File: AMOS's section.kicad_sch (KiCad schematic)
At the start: 0 parts

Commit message: Add Charging circuit and USB integration
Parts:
- added C1, C12: 4.7u, symbol Device:C_Small
- added D2: Red, symbol Device:LED_Small_Filled
- added D3: Green, symbol Device:LED_Small
- added J1: USB_C_Receptacle_PowerOnly_6P, Connector_USB:USB_C_Receptacle_HCTL_HC-TYPE-C-16P-01A, symbol Connector:USB_C_Receptacle_PowerOnly_6P
- added Q1: 2N2219, Package_TO_SOT_THT:TO-39-3, symbol Transistor_BJT:2N2219
- added R1, R16, R8: 1k, symbol Device:R_Small_US
- added R15: 3k, symbol Device:R_Small_US
- added R17: 10k, symbol Device:R_Small_US
- added R18: 6k8, symbol Device:R_Small_US
- added R9: 6k, symbol Device:R_Small_US
- added SW1: SW_Nidec_CAS-120A1, Button_Switch_SMD:Nidec_Copal_CAS-120A, symbol Switch:SW_Nidec_CAS-120A1
- added U6: TP4056-42-ESOP8, Package_SO:SOIC-8-1EP_3.9x4.9mm_P1.27mm_EP2.41x3.3mm_ThermalVias, symbol Battery_Management:TP4056-42-ESOP8
- added U7: CH224K, Package_SO:SSOP-10-1EP_3.9x4.9mm_P1mm_EP2.1x3.3mm, symbol Interface_USB:CH224K
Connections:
- new net: Q1.2 (B), R16.1
- new net: Q1.3 (C), R15.2
- new net: R15.1, R9.1, U6.2 (PROG)
- new net: D3.1 (K), U6.6 (~{STDBY})
- new net: D2.1 (K), U6.7 (~{CHRG})
- new net: D2.2 (A), R1.2
- new net: R18.1, U7.8 (VBUS)
- new net: D3.2 (A), R8.2
- new net 3V3: R17.2, U7.1 (VDD)
- new net Bat: C12.2, U6.5 (BAT)
- new net CC1: J1.A5 (CC1), U7.7 (CC1)
- new net CC2: J1.B5 (CC2), U7.6 (CC2)
- new net GND: C1.2, C12.1, J1.A12 (GND), J1.B12 (GND), Q1.1 (E), R9.2, U6.1 (TEMP), U6.3 (GND), U6.9 (EPAD), U7.11 (GND), U7.2 (CFG2), U7.3 (CFG3), U7.4 (DP), U7.5 (DM), U7.9 (CFG1)
- new net HV-Pin: C1.1, R1.1, R8.1, U6.4 (V_{CC}), U6.8 (CE)
- new net VBUS: J1.A9 (VBUS), J1.B9 (VBUS), R17.1, R18.2
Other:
- note added: "Charging Circuit"
- note added: "USb Integration"

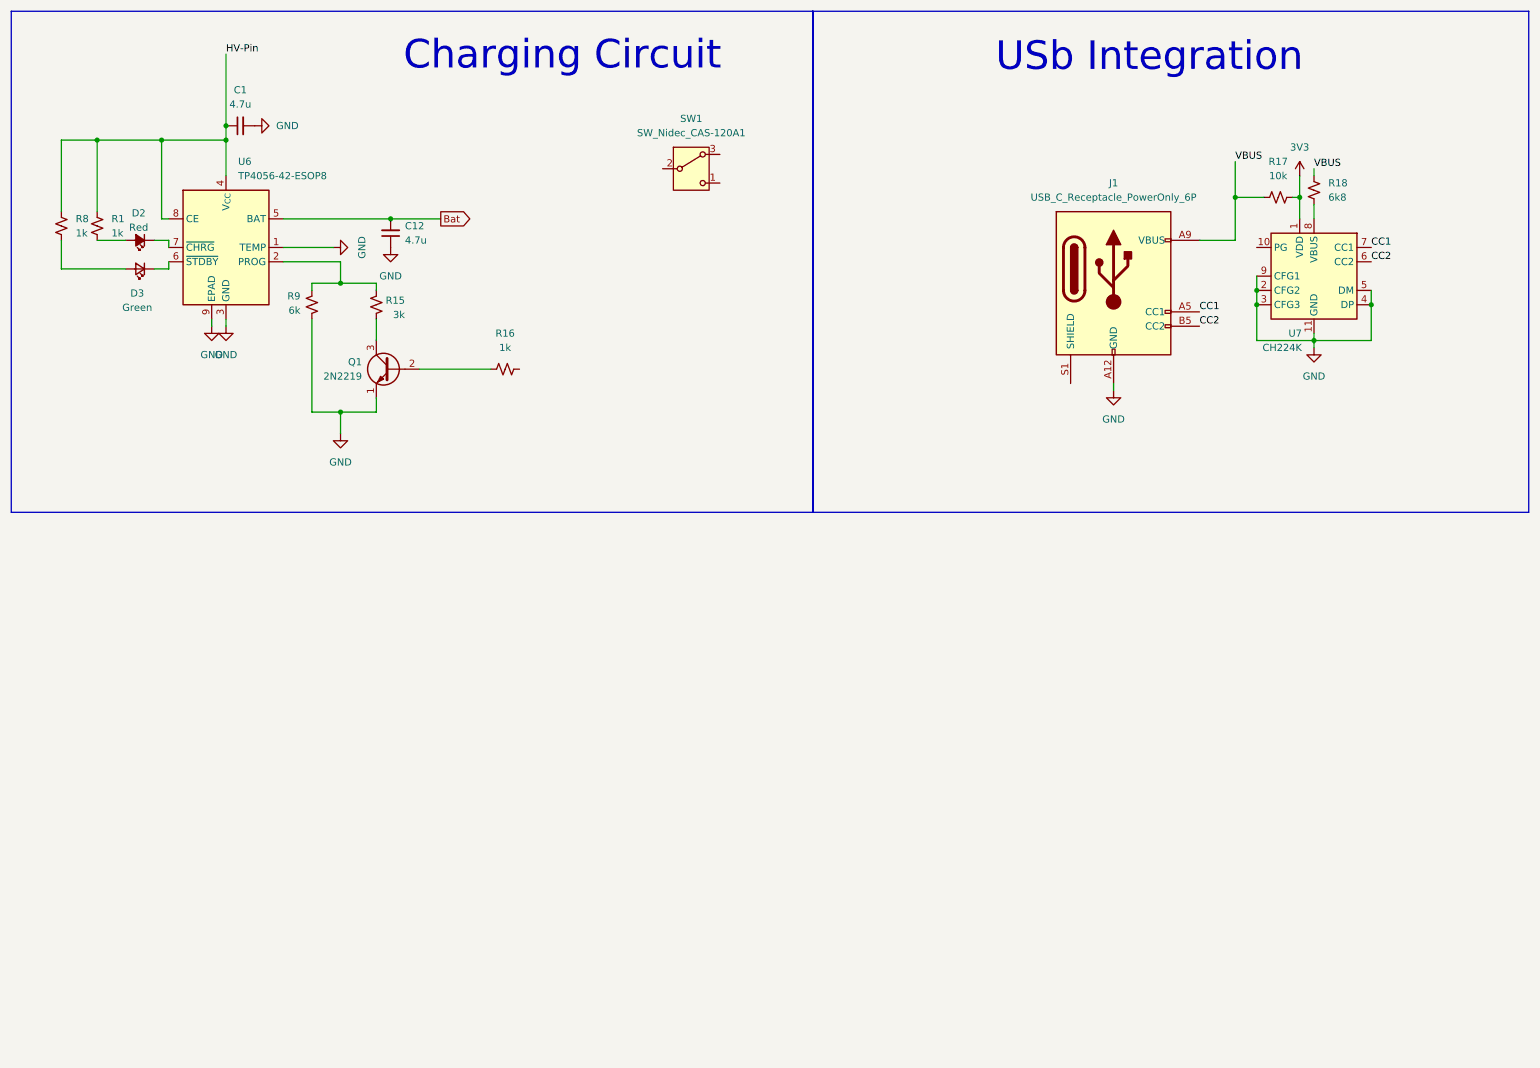
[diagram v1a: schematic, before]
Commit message: Add 2x16 connectors
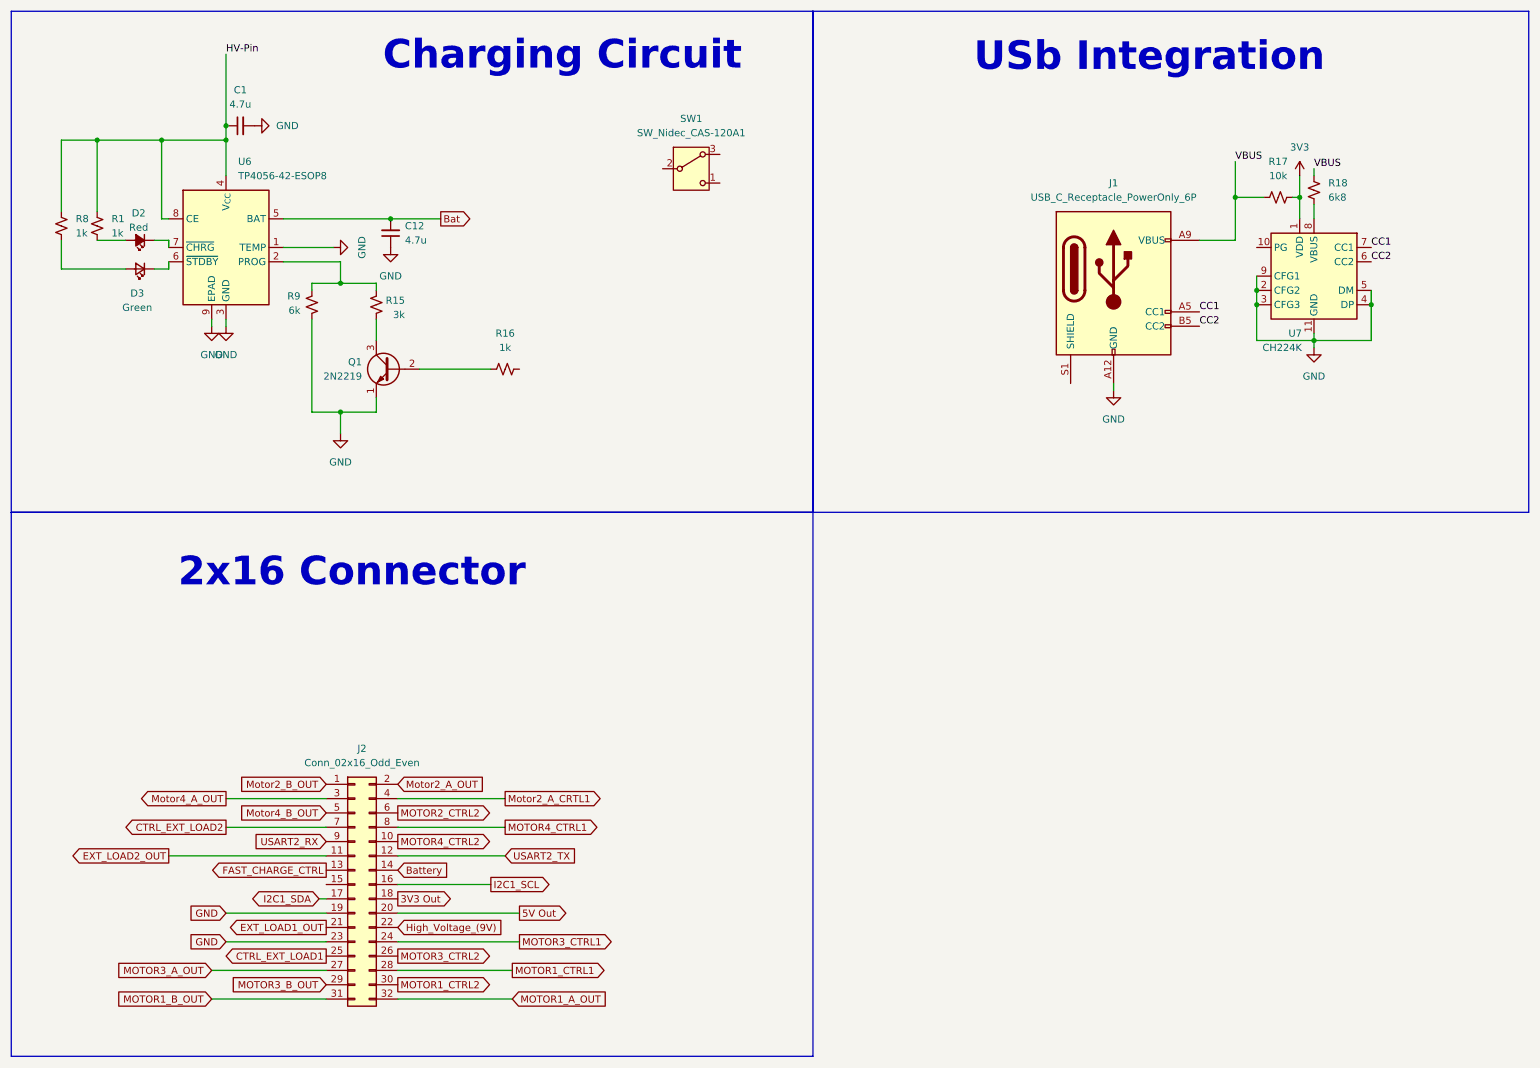
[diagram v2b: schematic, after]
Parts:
- added J2: Conn_02x16_Odd_Even, symbol Connector_Generic:Conn_02x16_Odd_Even
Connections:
- net GND: now also J2.19 (Pin_19), J2.23 (Pin_23)
- new net 3V3 Out: J2.18 (Pin_18)
- new net 5V Out: J2.20 (Pin_20)
- new net Battery: J2.14 (Pin_14)
- new net CTRL_EXT_LOAD1: J2.25 (Pin_25)
- new net CTRL_EXT_LOAD2: J2.7 (Pin_7)
- new net EXT_LOAD1_OUT: J2.21 (Pin_21)
- new net EXT_LOAD2_OUT: J2.11 (Pin_11)
- new net FAST_CHARGE_CTRL: J2.13 (Pin_13)
- new net High_Voltage_(9V): J2.22 (Pin_22)
- new net I2C1_SCL: J2.16 (Pin_16)
- new net I2C1_SDA: J2.17 (Pin_17)
- new net MOTOR1_A_OUT: J2.32 (Pin_32)
- new net MOTOR1_B_OUT: J2.31 (Pin_31)
- new net MOTOR1_CTRL1: J2.28 (Pin_28)
- new net MOTOR1_CTRL2: J2.30 (Pin_30)
- new net MOTOR2_CTRL2: J2.6 (Pin_6)
- new net MOTOR3_A_OUT: J2.27 (Pin_27)
- new net MOTOR3_B_OUT: J2.29 (Pin_29)
- new net MOTOR3_CTRL1: J2.24 (Pin_24)
- new net MOTOR3_CTRL2: J2.26 (Pin_26)
- new net MOTOR4_CTRL1: J2.8 (Pin_8)
- new net MOTOR4_CTRL2: J2.10 (Pin_10)
- new net Motor2_A_CRTL1: J2.4 (Pin_4)
- new net Motor2_A_OUT: J2.2 (Pin_2)
- new net Motor2_B_OUT: J2.1 (Pin_1)
- new net Motor4_A_OUT: J2.3 (Pin_3)
- new net Motor4_B_OUT: J2.5 (Pin_5)
- new net USART2_RX: J2.9 (Pin_9)
- new net USART2_TX: J2.12 (Pin_12)
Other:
- note added: "2x16 Connector"

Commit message: Add digital switch for fast charging
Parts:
- removed Q1: 2N2219, Package_TO_SOT_THT:TO-39-3, symbol Transistor_BJT:2N2219
- removed R16: 1k, symbol Device:R_Small_US
- removed SW1: SW_Nidec_CAS-120A1, Button_Switch_SMD:Nidec_Copal_CAS-120A, symbol Switch:SW_Nidec_CAS-120A1
- added U8: TS5A3159ADBVR, Package_TO_SOT_SMD:SOT-23-6, symbol Analog_Switch:TS5A3159ADBVR
- R15: value 3k -> 1k8
- R9: value 6k -> 5k5
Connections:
- net 3V3 is gone; now on net 3V3 Out: R17.2, U7.1 (VDD)
- net FAST_CHARGE_CTRL: now also U8.6
- net GND: now also U8.4; no longer R9.2
- net at R15.2: now also U8.1
- new net: R9.2, U8.3

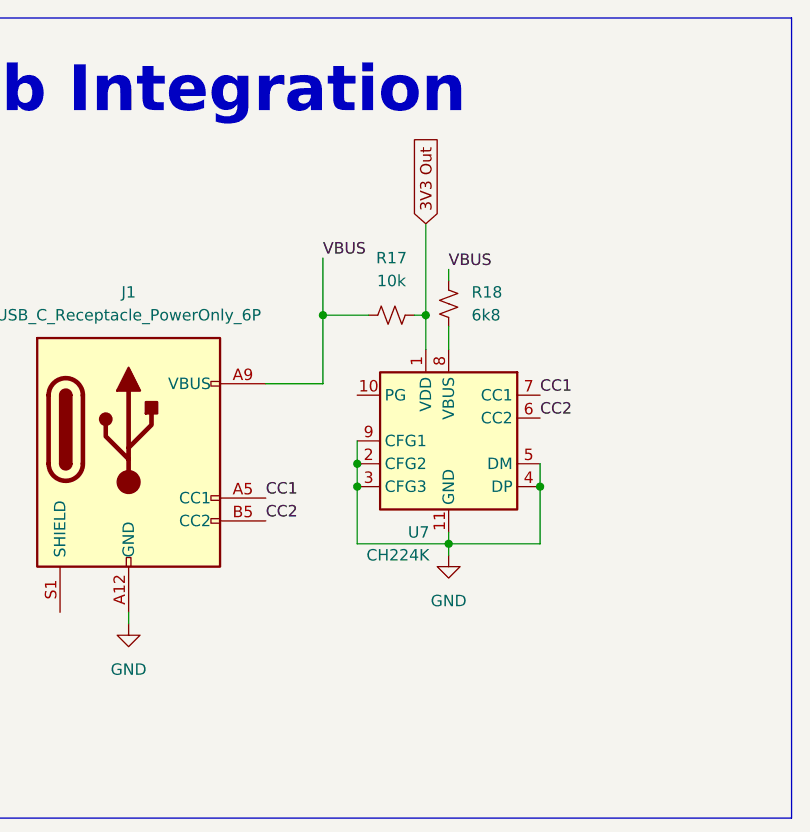
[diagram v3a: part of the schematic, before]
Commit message: Fix negotiator configuration
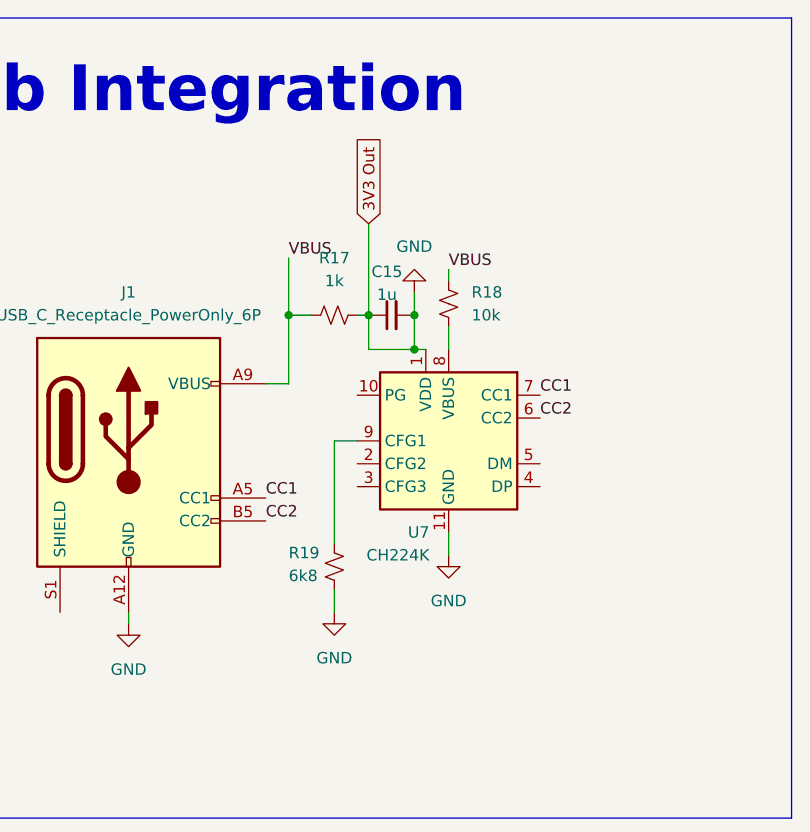
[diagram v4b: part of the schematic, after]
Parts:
- added C15: 1u, symbol Device:C_Small
- added R19: 6k8, symbol Device:R_Small_US
- R17: value 10k -> 1k
- R18: value 6k8 -> 10k
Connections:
- net 3V3 Out is gone; now on net GND: J2.18 (Pin_18), R17.2, U7.1 (VDD)
- net GND: now also C15.1, C15.2, R19.1; no longer U7.2 (CFG2), U7.3 (CFG3), U7.4 (DP), U7.5 (DM), U7.9 (CFG1)
- new net: R19.2, U7.9 (CFG1)
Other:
- moved on the sheet: R17
